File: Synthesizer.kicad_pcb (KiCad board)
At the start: 6 copper layers, 169 parts, among them J1 USB_A, J2 AudioJack3, J3 USB_B_Micro, J4 FPGA_debug, J5 MCU_debug, J6 67997-410HLF, SW1 SW_Push, SW10 SW_Push, SW11 SW_Push, SW12 SW_Push, SW13 SW_Push, SW14 SW_Push, SW15 SW_Push, SW16 SW_Push, SW2 SW_Push, SW3 SW_Push, SW4 SW_Push, SW5 SW_Push, SW6 SW_Push, SW7 SW_Push, SW8 SW_Push, SW9 SW_Push, U1 TPD3S014, U2 S25FL127S, U3 XC7A100T-FTG256, U4 Oscillator, U5 TPS54325, U6 TPS54294, U7 EFM32GG11B4xx, U8 PCM5102, Y1 48Mhz

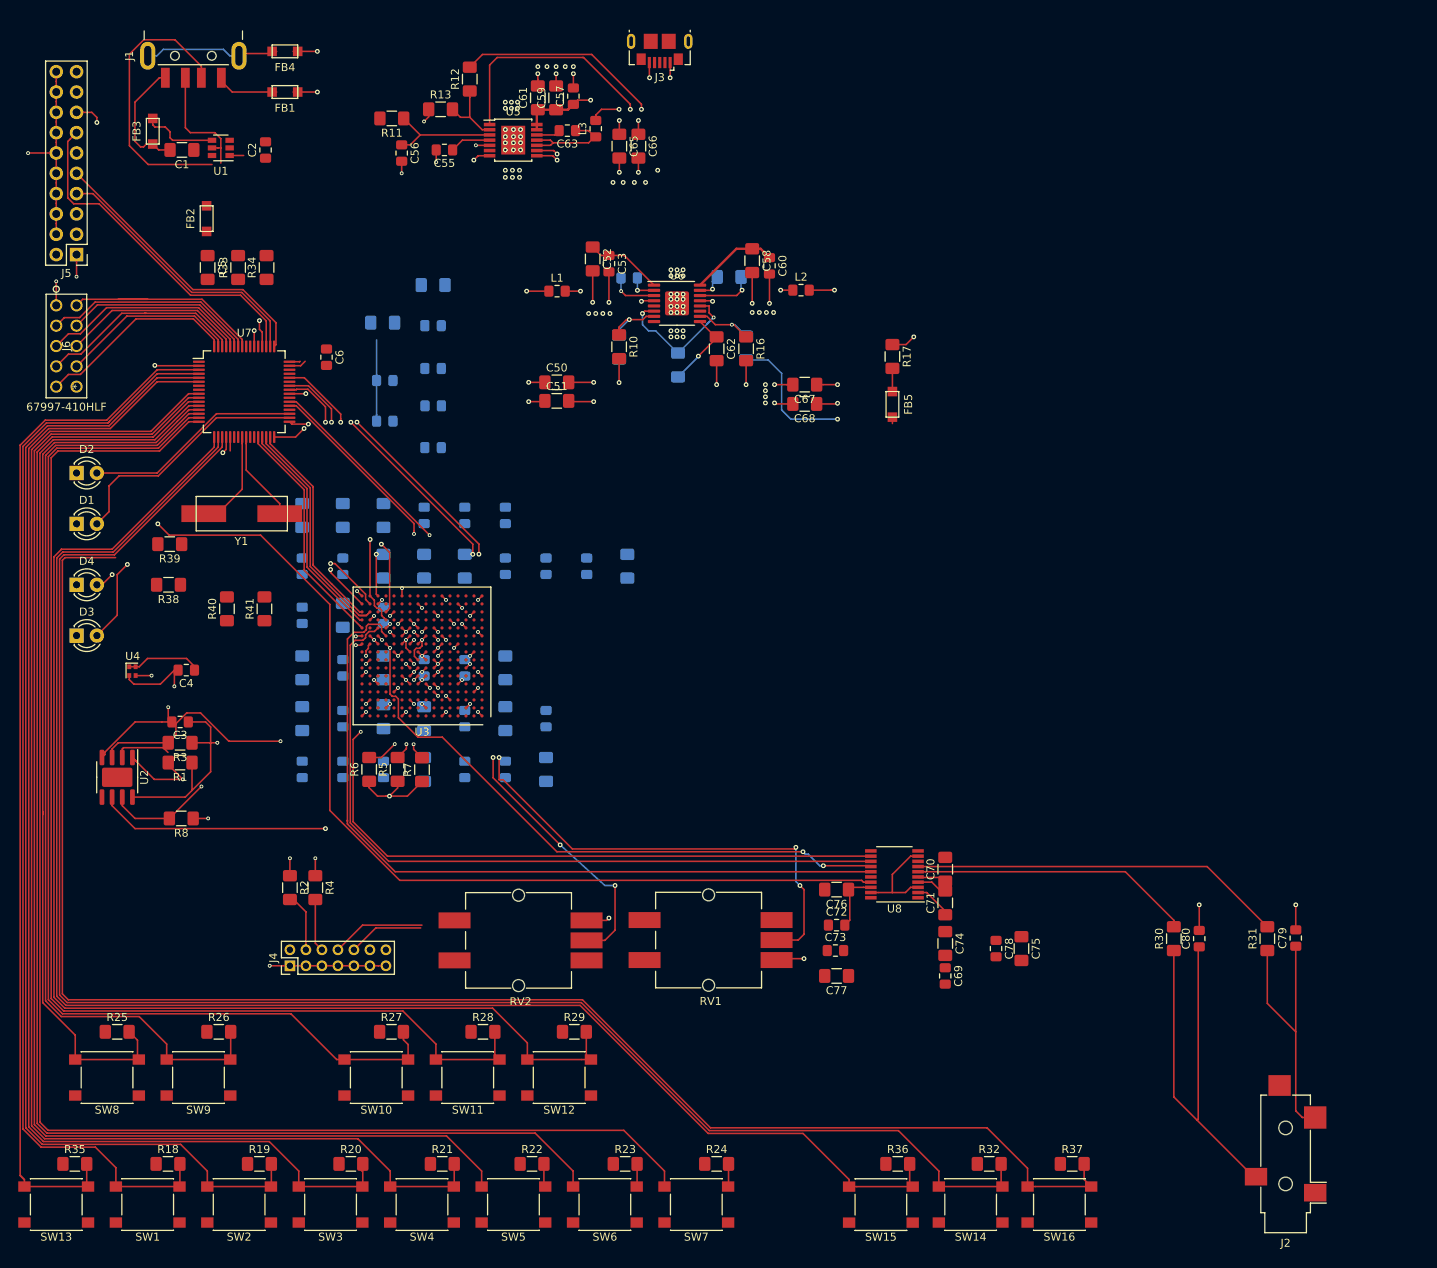
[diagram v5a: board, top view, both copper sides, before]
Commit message: Rearrange and rewire most of the PCB
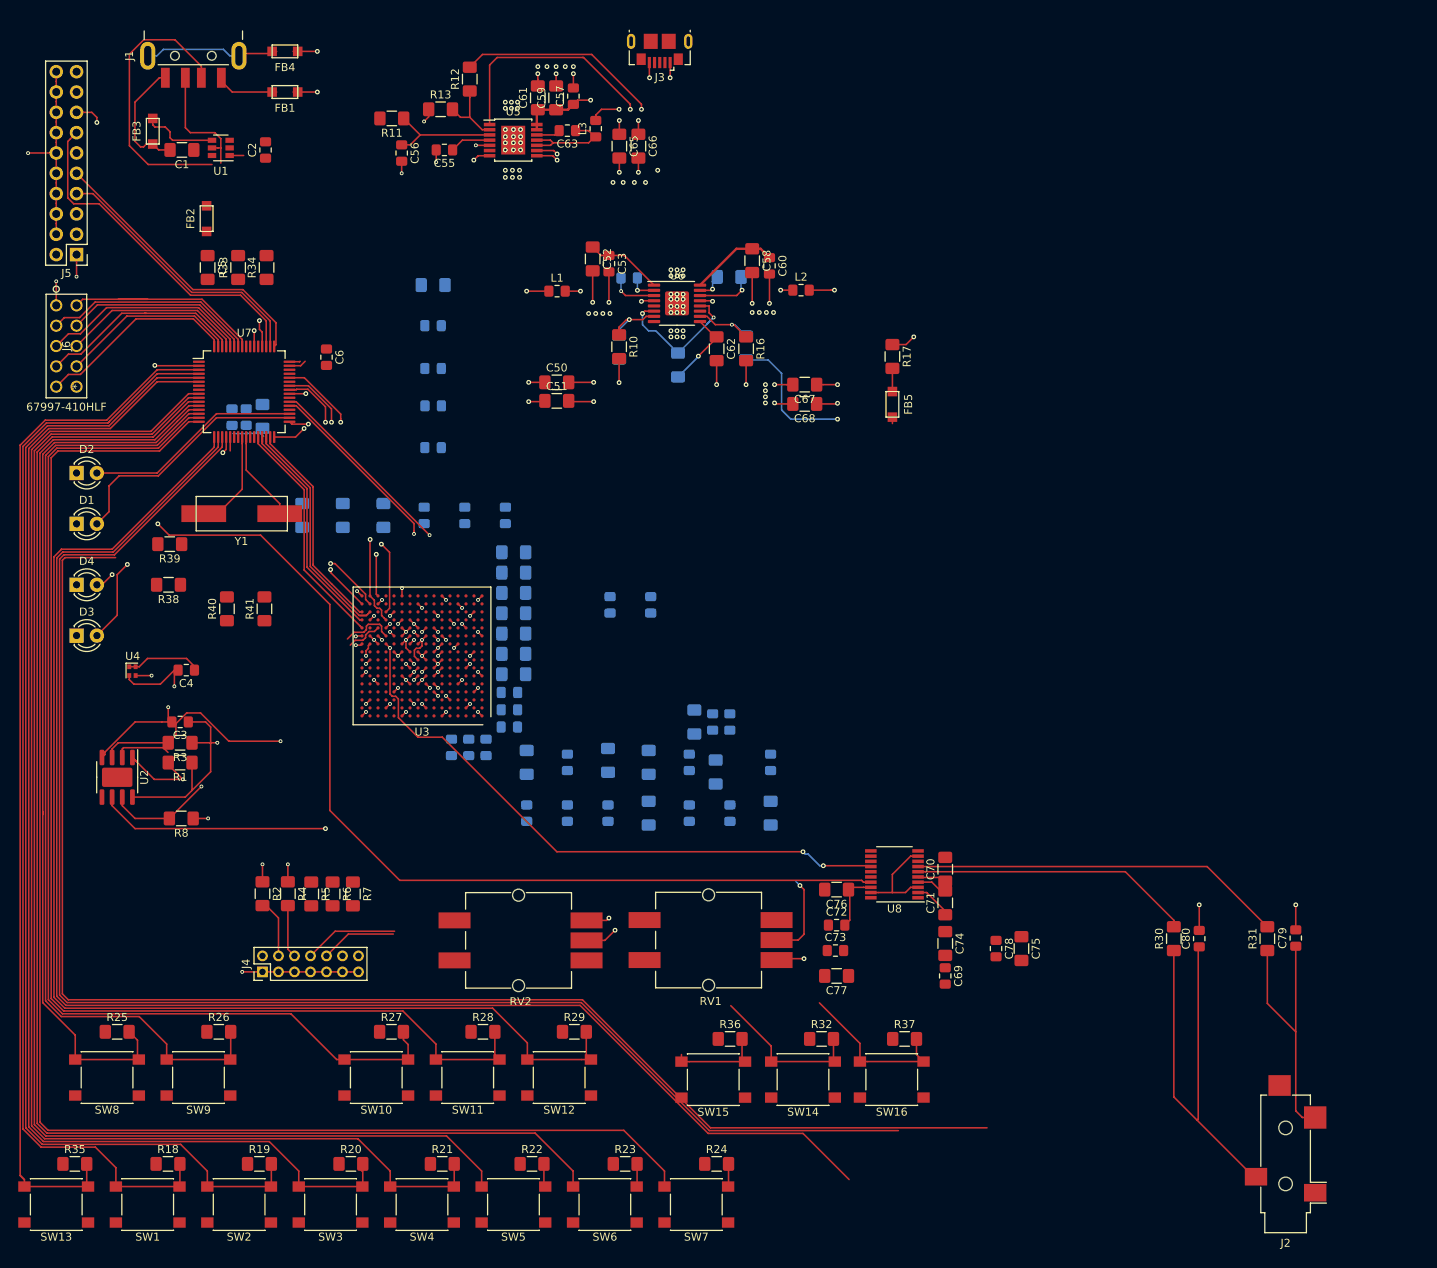
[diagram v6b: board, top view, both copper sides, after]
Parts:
- moved C22 55.1 mm to (102.0, 98.4)
- moved C13 45.9 mm to (97.5, 98.4)
- moved C18 43.3 mm to (99.8, 98.4)
- moved C40 32.3 mm to (71.5, 101.6)
- moved C24 28.6 mm to (107.1, 109.8)
- moved C43 28.6 mm to (107.1, 103.5)
- moved C30 28.6 mm to (81.7, 109.8)
- moved C34 28.6 mm to (76.6, 109.8)
- moved C41 28.6 mm to (91.8, 109.8)
- moved C47 28.6 mm to (86.8, 109.8)
- moved C15 28.6 mm to (91.8, 103.5)
- moved C19 28.6 mm to (86.8, 103.2)
- moved C27 28.6 mm to (76.6, 103.5)
- moved C32 28.6 mm to (81.7, 103.5)
- moved C45 28.6 mm to (96.9, 109.8)
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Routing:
- net /Artix7/DAC_LRCK: track 98.0 -> 6.82 mm
- net /Audio DAC/Bit-clock: track 93.8 -> 4.55 mm
- net /Artix7/DAC_SCK: track 91.4 -> 13.3 mm, vias 2 -> 1
- net +3V3: track 98.2 -> 87.3 mm, vias 21 -> 20
- net (no net): track 0.00 -> 10.1 mm
- net +3.3VA: track 13.2 -> 7.04 mm
- net /EFM32/FPGA_Reset: track 55.3 -> 51.4 mm, vias 3 -> 2
- net Net-(RV1-Pad2): track 120.4 -> 118.2 mm, vias 6 -> 2
- net Net-(R5-Pad2): track 16.2 -> 14.1 mm, vias 2 -> 1
- net /EFM32/FPGA_Ready: track 54.6 -> 52.5 mm, vias 3 -> 2
- net Net-(RV2-Pad2): track 91.5 -> 90.6 mm, vias 6 -> 2

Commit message: Rearrange and wire most of PCB FOR REAL THIS TIME
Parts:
- added J7: 67997-410HLF, footprints:67997-410HLF, F.Cu at (166.2, 92.9)
- moved U4 115.4 mm to (142.6, 96.2), turned to 270 degrees
- moved J5 114.5 mm to (115.2, 104.1), turned to 270 degrees
- moved C4 108.6 mm to (142.6, 94.3)
- moved D4 107.1 mm to (126.1, 98.1)
- moved D3 105.9 mm to (126.1, 92.6)
- moved SW13 105.5 mm to (56.9, 60.8), turned to 90 degrees
- moved C14 105.2 mm to (151.1, 96.0), turned to 0 degrees
- moved U2 104.9 mm to (130.3, 107.0), turned to 90 degrees
- moved C35 100.3 mm to (174.1, 105.8), turned to 270 degrees
- moved C20 99.7 mm to (151.1, 93.6), turned to 0 degrees
- moved R2 99.4 mm to (137.6, 87.9), turned to 180 degrees
- moved R35 99.3 mm to (61.4, 63.4), turned to 270 degrees
- moved R5 98.5 mm to (148.2, 119.1), turned to 90 degrees
- moved J4 98.2 mm to (131.5, 85.9), turned to 0 degrees
- moved C37 98.1 mm to (172.1, 105.8), turned to 270 degrees
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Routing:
- net +3V3: track 87.3 -> 500.5 mm, vias 20 -> 21
- net /Button14: track 212.9 -> 10.2 mm
- net /Button15: track 205.8 -> 10.2 mm
- net /Button13: track 202.3 -> 10.2 mm
- net /Button7: track 191.3 -> 10.2 mm
- net /Button6: track 181.0 -> 10.2 mm
- net /Button5: track 170.7 -> 10.2 mm
- net /Button4: track 168.3 -> 10.3 mm
- net /Button3: track 158.5 -> 10.2 mm
- net /Button12: track 157.6 -> 10.4 mm
- net /Button11: track 152.2 -> 10.4 mm
- net /Button2: track 148.2 -> 10.4 mm
- net /Button10: track 140.5 -> 10.2 mm
- net /Button1: track 138.1 -> 10.4 mm
- net /Button0: track 130.7 -> 10.2 mm
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- removed copper zone on PWR_plane, net +1V0
- removed copper zone on PWR_plane, net +1V8
- removed copper zone on PWR_plane, net +3V3
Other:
- board outline added: 135.2 x 94.2 mm
- board text removed: "5V might need thicker trace"

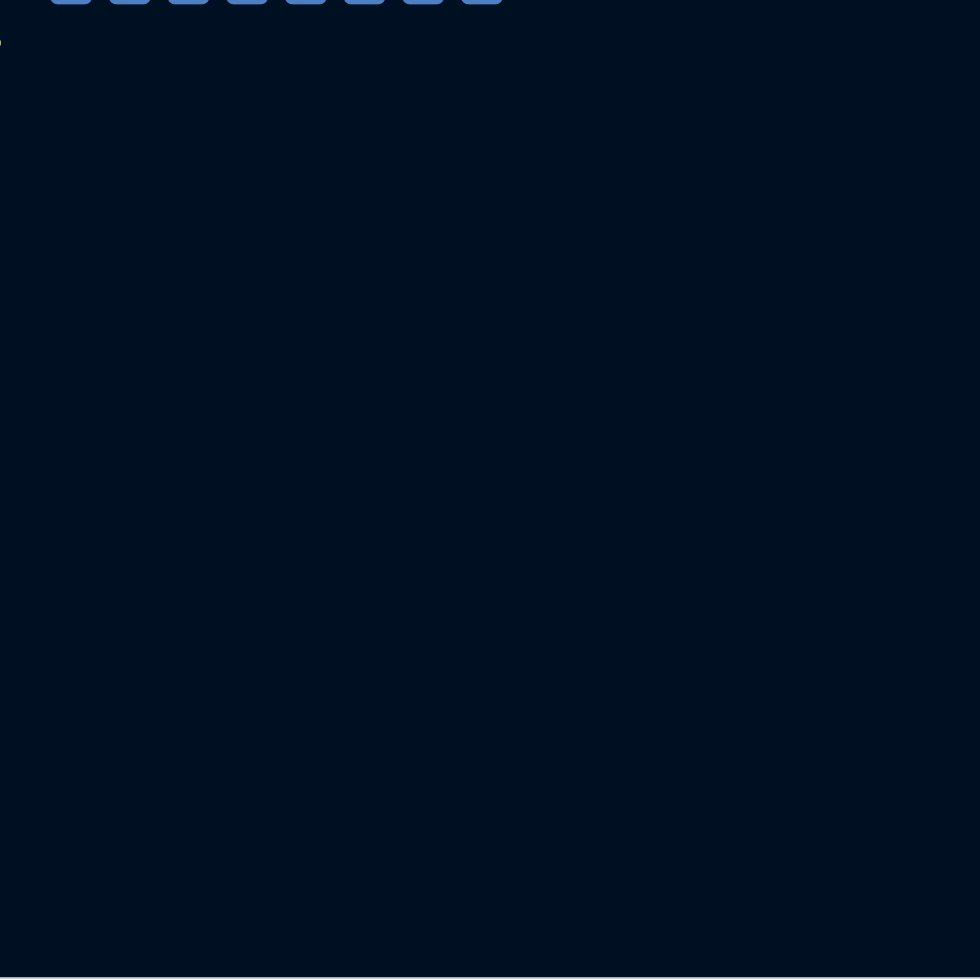
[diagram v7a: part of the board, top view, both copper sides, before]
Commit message: Readd logo
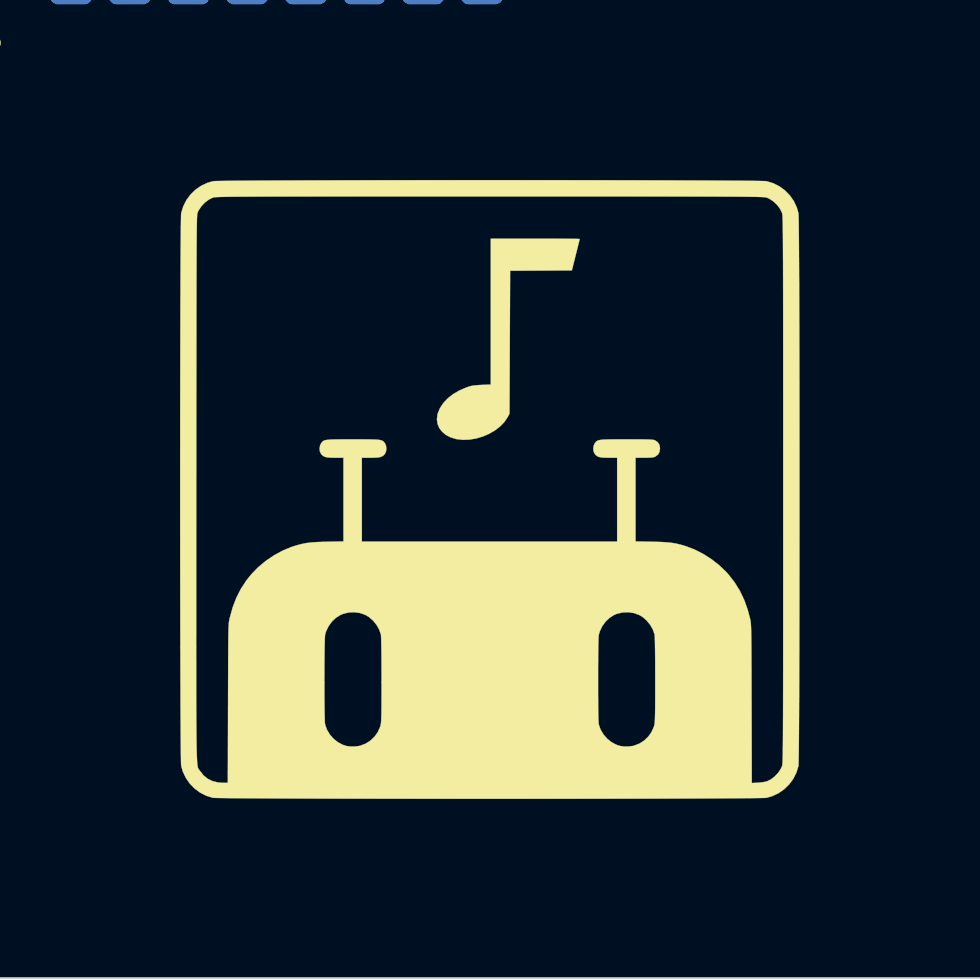
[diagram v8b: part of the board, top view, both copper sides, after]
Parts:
- added G***: LOGO, footprints:synthlogo, F.Cu at (170.2, 132.3)
